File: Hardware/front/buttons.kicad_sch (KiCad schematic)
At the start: 40 parts

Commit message: Start routing front panel stuff
- Routed some of the LED driver pins and replaced footprints of passives
  with 0603 size to match the controller board
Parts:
- U: MPN CR0805-JW-102ELF -> (none)
- U: MPN CL21A475KAQNNNF -> (none)
- U: MPN RMC1/10-103JTP -> (none)
- U: MPN CL21B104KACNFNC -> (none)
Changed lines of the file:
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@@
       (effects (font (size 1.27 1.27)) hide)
     )
-    (property "MPN" "CR0805-JW-102ELF" (id 4) (at 33.655 31.115 0)
+    (property "MPN" "" (id 4) (at 33.655 31.115 0)
       (effects (font (size 1.27 1.27)) hide)
     )
@@
       (effects (font (size 1.27 1.27)) hide)
     )
-    (property "MPN" "CR0805-JW-102ELF" (id 4) (at 223.52 34.925 0)
+    (property "MPN" "" (id 4) (at 223.52 34.925 0)
       (effects (font (size 1.27 1.27)) hide)
     )
@@
       (effects (font (size 1.27 1.27)) hide)
     )
-    (property "MPN" "CR0805-JW-102ELF" (id 4) (at 33.655 88.265 0)
+    (property "MPN" "" (id 4) (at 33.655 88.265 0)
       (effects (font (size 1.27 1.27)) hide)
     )
@@
       (effects (font (size 1.27 1.27)) hide)
     )
-    (property "MPN" "CR0805-JW-102ELF" (id 4) (at 212.09 69.85 90)
+    (property "MPN" "" (id 4) (at 212.09 69.85 90)
       (effects (font (size 1.27 1.27)) hide)
     )
@@
       (effects (font (size 1.27 1.27)) hide)
     )
-    (property "MPN" "CL21A475KAQNNNF" (id 4) (at 61.595 85.09 0)
+    (property "MPN" "" (id 4) (at 61.595 85.09 0)
       (effects (font (size 1.27 1.27)) hide)
     )
@@
       (effects (font (size 1.27 1.27)) hide)
     )
-    (property "MPN" "RMC1/10-103JTP" (id 4) (at 215.265 34.925 0)
+    (property "MPN" "" (id 4) (at 215.265 34.925 0)
       (effects (font (size 1.27 1.27)) hide)
     )
@@
       (effects (font (size 1.27 1.27)) hide)
     )
-    (property "MPN" "RMC1/10-103JTP" (id 4) (at 25.4 69.215 0)
+    (property "MPN" "" (id 4) (at 25.4 69.215 0)
       (effects (font (size 1.27 1.27)) hide)
     )
@@
       (effects (font (size 1.27 1.27)) hide)
     )
-    (property "MPN" "RMC1/10-103JTP" (id 4) (at 167.64 49.53 90)
+    (property "MPN" "" (id 4) (at 167.64 49.53 90)
       (effects (font (size 1.27 1.27)) hide)
     )
@@
       (effects (font (size 1.27 1.27)) hide)
     )
-    (property "MPN" "CR0805-JW-102ELF" (id 4) (at 33.655 50.165 0)
+    (property "MPN" "" (id 4) (at 33.655 50.165 0)
       (effects (font (size 1.27 1.27)) hide)
     )
@@
       (effects (font (size 1.27 1.27)) hide)
     )
-    (property "MPN" "CL21A475KAQNNNF" (id 4) (at 61.595 27.94 0)
+    (property "MPN" "" (id 4) (at 61.595 27.94 0)
       (effects (font (size 1.27 1.27)) hide)
     )
@@
       (effects (font (size 1.27 1.27)) hide)
     )
-    (property "MPN" "CR0805-JW-102ELF" (id 4) (at 33.655 69.215 0)
+    (property "MPN" "" (id 4) (at 33.655 69.215 0)
       (effects (font (size 1.27 1.27)) hide)
     )
@@
       (effects (font (size 1.27 1.27)) hide)
     )
-    (property "MPN" "CR0805-JW-102ELF" (id 4) (at 33.655 118.11 0)
+    (property "MPN" "" (id 4) (at 33.655 118.11 0)
       (effects (font (size 1.27 1.27)) hide)
     )
@@
       (effects (font (size 1.27 1.27)) hide)
     )
-    (property "MPN" "RMC1/10-103JTP" (id 4) (at 25.4 118.11 0)
+    (property "MPN" "" (id 4) (at 25.4 118.11 0)
       (effects (font (size 1.27 1.27)) hide)
     )
@@
       (effects (font (size 1.27 1.27)) hide)
     )
-    (property "MPN" "RMC1/10-103JTP" (id 4) (at 222.885 66.04 0)
+    (property "MPN" "" (id 4) (at 222.885 66.04 0)
       (effects (font (size 1.27 1.27)) hide)
     )
@@
       (effects (font (size 1.27 1.27)) hide)
     )
-    (property "MPN" "CL21A475KAQNNNF" (id 4) (at 200.025 72.39 0)
+    (property "MPN" "" (id 4) (at 200.025 72.39 0)
       (effects (font (size 1.27 1.27)) hide)
     )
@@
       (effects (font (size 1.27 1.27)) hide)
     )
-    (property "MPN" "CL21A475KAQNNNF" (id 4) (at 61.595 114.935 0)
+    (property "MPN" "" (id 4) (at 61.595 114.935 0)
       (effects (font (size 1.27 1.27)) hide)
     )
@@
       (effects (font (size 1.27 1.27)) hide)
     )
-    (property "MPN" "CL21B104KACNFNC" (id 4) (at 186.69 93.345 0)
+    (property "MPN" "" (id 4) (at 186.69 93.345 0)
       (effects (font (size 1.27 1.27)) hide)
     )
@@
       (effects (font (size 1.27 1.27)) hide)
     )
-    (property "MPN" "RMC1/10-103JTP" (id 4) (at 167.64 40.64 90)
+    (property "MPN" "" (id 4) (at 167.64 40.64 90)
       (effects (font (size 1.27 1.27)) hide)
     )
@@
       (effects (font (size 1.27 1.27)) hide)
     )
-    (property "MPN" "CL21A475KAQNNNF" (id 4) (at 61.595 66.04 0)
+    (property "MPN" "" (id 4) (at 61.595 66.04 0)
       (effects (font (size 1.27 1.27)) hide)
     )
@@
       (effects (font (size 1.27 1.27)) hide)
     )
-    (property "MPN" "CL21A475KAQNNNF" (id 4) (at 61.595 46.99 0)
+    (property "MPN" "" (id 4) (at 61.595 46.99 0)
       (effects (font (size 1.27 1.27)) hide)
     )
@@
       (effects (font (size 1.27 1.27)) hide)
     )
-    (property "MPN" "CL21B104KACNFNC" (id 4) (at 73.66 177.165 0)
+    (property "MPN" "" (id 4) (at 73.66 177.165 0)
       (effects (font (size 1.27 1.27)) hide)
     )
@@
       (effects (font (size 1.27 1.27)) hide)
     )
-    (property "MPN" "RMC1/10-103JTP" (id 4) (at 25.4 31.115 0)
+    (property "MPN" "" (id 4) (at 25.4 31.115 0)
       (effects (font (size 1.27 1.27)) hide)
     )
@@
       (effects (font (size 1.27 1.27)) hide)
     )
-    (property "MPN" "RMC1/10-103JTP" (id 4) (at 25.4 50.165 0)
+    (property "MPN" "" (id 4) (at 25.4 50.165 0)
       (effects (font (size 1.27 1.27)) hide)
     )
@@
       (effects (font (size 1.27 1.27)) hide)
     )
-    (property "MPN" "RMC1/10-103JTP" (id 4) (at 25.4 88.265 0)
+    (property "MPN" "" (id 4) (at 25.4 88.265 0)
       (effects (font (size 1.27 1.27)) hide)
     )
@@
       (effects (font (size 1.27 1.27)) hide)
     )
-    (property "MPN" "CL21A475KAQNNNF" (id 4) (at 198.12 34.29 0)
-      (effects (font (size 1.27 1.27)) hide)
-    )
+    (property "MPN" "" (id 4) (at 198.12 34.29 0)
+      (effects (font (size 1.27 1.27)) hide)
+    )

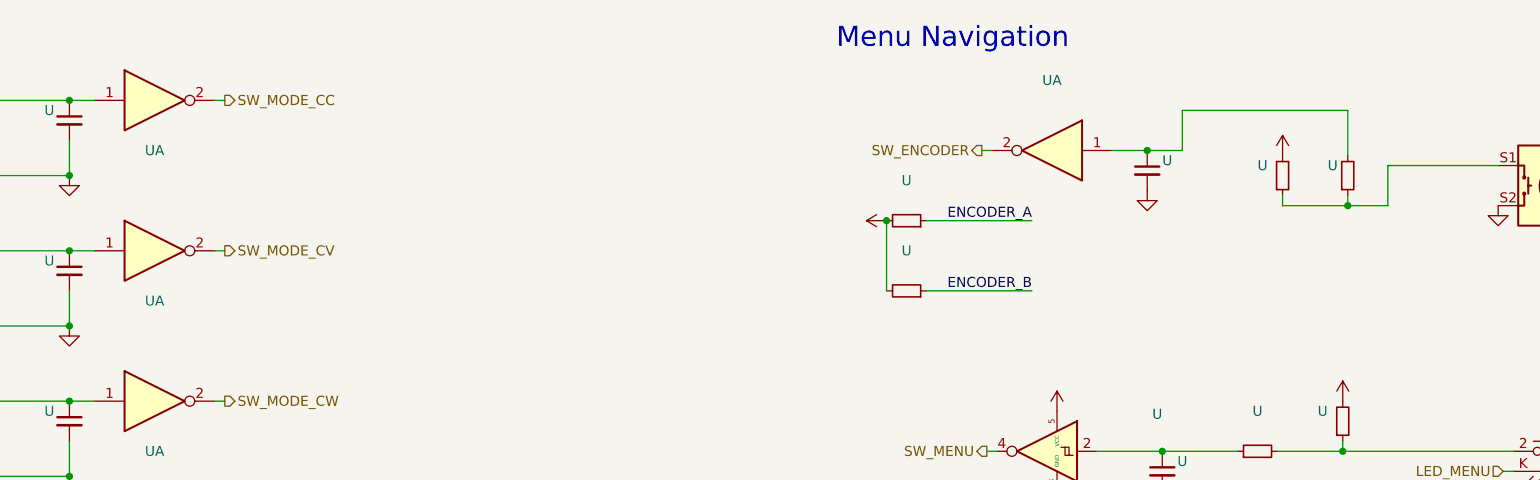
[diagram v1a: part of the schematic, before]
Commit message: Finished routing front panel
- Finished routing the contents of the front panel; it could probably
  use an optimization pass and general cleanup.

  A few of the assignments of IOs/LED driver outputs were changed as
  well to make the routing less of a pain in the ass, as compared to the
  previous front panels.

- Minor tweaks to controller to remove some unused signals
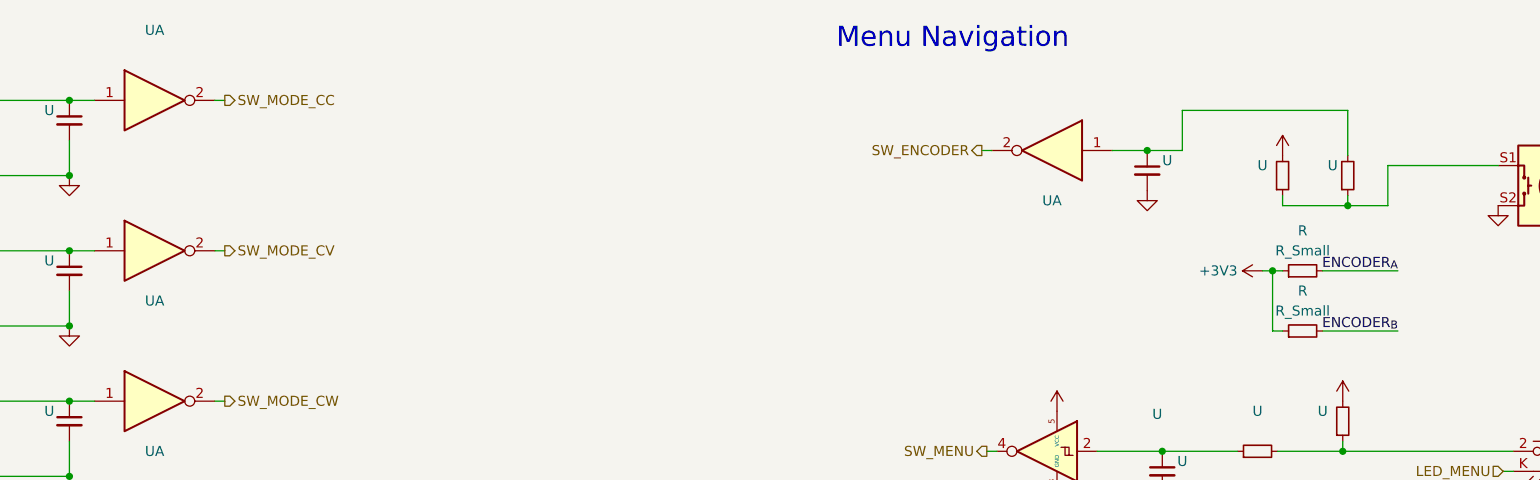
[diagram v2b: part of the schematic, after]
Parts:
- removed U (x2): (no value), symbol Device:R_Small
- added R (x2): R_Small, symbol Device:R_Small
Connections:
- net +3V3: now also R.1, R.1
- net ENCODER_{A}: now also R.2
- net ENCODER_{B}: now also R.2
- net SW_ENCODER: now also U.2; no longer U.2
- net SW_MODE_CC: now also U.2; no longer U.2
- net SW_MODE_CV: now also U.2; no longer U.2
- net SW_MODE_CW: now also U.2; no longer U.2
- net at U.1, U.2: now also U.1; no longer U.1 (x4)
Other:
- moved on the sheet: UA

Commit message: updated front panel pinout
- added system reset, direct load on/off switch output lines

- added separate touch screen reset/interrupt lines (the touch
  controller gets to be driven by linux side)

- update footprint for ER-TFT040-1 display

  this tweaks the sizes of the openings and the text labels a bit to be
  prettier
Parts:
- R, U: JLCPCB (none) -> C25804
- U: JLCPCB (none) -> C21190
- U: JLCPCB (none) -> C19666
- U: JLCPCB (none) -> C14663
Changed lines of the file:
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@@
+      (effects (font (size 1.27 1.27)) hide)
+    )
+    (property "JLCPCB" "C21190" (id 5) (at 33.655 31.115 0)
       (effects (font (size 1.27 1.27)) hide)
     )
@@
       (effects (font (size 1.27 1.27)) hide)
     )
+    (property "JLCPCB" "C21190" (id 5) (at 223.52 34.925 0)
+      (effects (font (size 1.27 1.27)) hide)
+    )
     (pin "1")
     (pin "2")
@@
     )
     (property "MPN" "" (id 4) (at 33.655 88.265 0)
+      (effects (font (size 1.27 1.27)) hide)
+    )
+    (property "JLCPCB" "C21190" (id 5) (at 33.655 88.265 0)
       (effects (font (size 1.27 1.27)) hide)
     )
@@
       (effects (font (size 1.27 1.27)) hide)
     )
+    (property "JLCPCB" "C21190" (id 5) (at 212.09 69.85 90)
+      (effects (font (size 1.27 1.27)) hide)
+    )
     (pin "1")
     (pin "2")
@@
       (effects (font (size 1.27 1.27)) hide)
     )
+    (property "JLCPCB" "C19666" (id 5) (at 61.595 85.09 0)
+      (effects (font (size 1.27 1.27)) hide)
+    )
     (pin "1")
     (pin "2")
@@
       (effects (font (size 1.27 1.27)) hide)
     )
+    (property "JLCPCB" "C25804" (id 5) (at 215.265 34.925 0)
+      (effects (font (size 1.27 1.27)) hide)
+    )
     (pin "1")
     (pin "2")
@@
       (effects (font (size 1.27 1.27)) hide)
     )
+    (property "JLCPCB" "C25804" (id 4) (at 217.805 46.99 90)
+      (effects (font (size 1.27 1.27)) hide)
+    )
     (pin "1")
     (pin "2")
@@
     )
     (property "MPN" "" (id 4) (at 25.4 69.215 0)
+      (effects (font (size 1.27 1.27)) hide)
+    )
+    (property "JLCPCB" "C25804" (id 5) (at 25.4 69.215 0)
       (effects (font (size 1.27 1.27)) hide)
     )
@@
       (effects (font (size 1.27 1.27)) hide)
     )
+    (property "JLCPCB" "C21190" (id 5) (at 33.655 50.165 0)
+      (effects (font (size 1.27 1.27)) hide)
+    )
     (pin "1")
     (pin "2")
@@
     )
     (property "MPN" "" (id 4) (at 61.595 27.94 0)
+      (effects (font (size 1.27 1.27)) hide)
+    )
+    (property "JLCPCB" "C19666" (id 5) (at 61.595 27.94 0)
       (effects (font (size 1.27 1.27)) hide)
     )
@@
       (effects (font (size 1.27 1.27)) hide)
     )
+    (property "JLCPCB" "C25804" (id 4) (at 217.805 54.61 90)
+      (effects (font (size 1.27 1.27)) hide)
+    )
     (pin "1")
     (pin "2")
@@
     )
     (property "MPN" "" (id 4) (at 33.655 69.215 0)
+      (effects (font (size 1.27 1.27)) hide)
+    )
+    (property "JLCPCB" "C21190" (id 5) (at 33.655 69.215 0)
       (effects (font (size 1.27 1.27)) hide)
     )
@@
       (effects (font (size 1.27 1.27)) hide)
     )
+    (property "JLCPCB" "C21190" (id 5) (at 33.655 118.11 0)
+      (effects (font (size 1.27 1.27)) hide)
+    )
     (pin "1")
     (pin "2")
@@
       (effects (font (size 1.27 1.27)) hide)
     )
+    (property "JLCPCB" "C25804" (id 5) (at 25.4 118.11 0)
+      (effects (font (size 1.27 1.27)) hide)
+    )
     (pin "1")
     (pin "2")
@@
       (effects (font (size 1.27 1.27)) hide)
     )
+    (property "JLCPCB" "C25804" (id 5) (at 222.885 66.04 0)
+      (effects (font (size 1.27 1.27)) hide)
+    )
     (pin "1")
     (pin "2")
@@
       (effects (font (size 1.27 1.27)) hide)
     )
+    (property "JLCPCB" "C19666" (id 5) (at 200.025 72.39 0)
+      (effects (font (size 1.27 1.27)) hide)
+    )
     (pin "1")
     (pin "2")
@@
     )
     (property "MPN" "" (id 4) (at 61.595 114.935 0)
+      (effects (font (size 1.27 1.27)) hide)
+    )
+    (property "JLCPCB" "C19666" (id 5) (at 61.595 114.935 0)
       (effects (font (size 1.27 1.27)) hide)
     )
@@
       (effects (font (size 1.27 1.27)) hide)
     )
+    (property "JLCPCB" "C14663" (id 5) (at 186.69 93.345 0)
+      (effects (font (size 1.27 1.27)) hide)
+    )
     (pin "1")
     (pin "2")
@@
       (effects (font (size 1.27 1.27)) hide)
     )
+    (property "JLCPCB" "C19666" (id 5) (at 61.595 66.04 0)
+      (effects (font (size 1.27 1.27)) hide)
+    )
     (pin "1")
     (pin "2")
@@
     )
     (property "MPN" "" (id 4) (at 61.595 46.99 0)
+      (effects (font (size 1.27 1.27)) hide)
+    )
+    (property "JLCPCB" "C19666" (id 5) (at 61.595 46.99 0)
       (effects (font (size 1.27 1.27)) hide)
     )
@@
       (effects (font (size 1.27 1.27)) hide)
     )
+    (property "JLCPCB" "C14663" (id 5) (at 73.66 177.165 0)
+      (effects (font (size 1.27 1.27)) hide)
+    )
     (pin "1")
     (pin "2")
@@
     )
     (property "MPN" "" (id 4) (at 25.4 31.115 0)
+      (effects (font (size 1.27 1.27)) hide)
+    )
+    (property "JLCPCB" "C25804" (id 5) (at 25.4 31.115 0)
       (effects (font (size 1.27 1.27)) hide)
     )
@@
       (effects (font (size 1.27 1.27)) hide)
     )
+    (property "JLCPCB" "C25804" (id 5) (at 25.4 50.165 0)
+      (effects (font (size 1.27 1.27)) hide)
+    )
     (pin "1")
     (pin "2")
@@
     )
     (property "MPN" "" (id 4) (at 25.4 88.265 0)
+      (effects (font (size 1.27 1.27)) hide)
+    )
+    (property "JLCPCB" "C25804" (id 5) (at 25.4 88.265 0)
       (effects (font (size 1.27 1.27)) hide)
     )
@@
       (effects (font (size 1.27 1.27)) hide)
     )
+    (property "JLCPCB" "C19666" (id 5) (at 198.12 34.29 0)
+      (effects (font (size 1.27 1.27)) hide)
+    )
